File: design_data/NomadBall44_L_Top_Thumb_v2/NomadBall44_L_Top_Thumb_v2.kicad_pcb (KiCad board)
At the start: 2 copper layers, 65.4 x 33.6 mm, 5 parts, among them SW21 SW_Push, SW22 SW_Push, SW23 SW_Push

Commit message: トッププレートのネジ穴フットプリントを変更
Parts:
- REF** (x2): footprint NomadBall44:m2_Screw_Hole_EdgeCuts -> NomadBall44:m2_Screw_Hole
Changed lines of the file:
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@@
 	)
 	(net 0 "")
-	(footprint "NomadBall44:m2_Screw_Hole_EdgeCuts"
+	(footprint "NomadBall44:m2_Screw_Hole"
 		(layer "F.Cu")
 		(at 230.94 119.92)
@@
 			(at 0 -3.2 0)
 			(layer "F.Fab")
-			(hide yes)
 			(effects
 				(font
@@
 			(at 0 3.2 0)
 			(layer "F.Fab")
-			(hide yes)
 			(effects
 				(font
@@
 		(fp_circle
 			(center 0 0)
-			(end 1.1 0)
-			(stroke
-				(width 0.01)
+			(end 2.2 0)
+			(stroke
+				(width 0.15)
 				(type solid)
 			)
 			(fill no)
-			(layer "Edge.Cuts")
+			(layer "Cmts.User")
+		)
+		(fp_circle
+			(center 0 0)
+			(end 2.45 0)
+			(stroke
+				(width 0.05)
+				(type solid)
+			)
+			(fill no)
+			(layer "F.CrtYd")
 		)
 		(fp_text user "${REFERENCE}"
-			(at 0 0 0)
-			(layer "F.Fab")
-			(effects
-				(font
-					(size 1 1)
-					(thickness 0.15)
-				)
-			)
+			(at 0.3 0 0)
+			(layer "F.Fab")
+			(effects
+				(font
+					(size 1 1)
+					(thickness 0.15)
+				)
+			)
+		)
+		(pad "" np_thru_hole circle
+			(at 0 0)
+			(size 2.2 2.2)
+			(drill 2.2)
+			(layers "*.Cu" "*.Mask")
 		)
 		(embedded_fonts no)
@@
 		(embedded_fonts no)
 	)
-	(footprint "NomadBall44:m2_Screw_Hole_EdgeCuts"
+	(footprint "NomadBall44:m2_Screw_Hole"
 		(layer "F.Cu")
 		(at 258.434757 133.419999)
@@
 			(at 0 -3.2 0)
 			(layer "F.Fab")
-			(hide yes)
 			(effects
 				(font
@@
 			(at 0 3.2 0)
 			(layer "F.Fab")
-			(hide yes)
 			(effects
 				(font
@@
 		(fp_circle
 			(center 0 0)
-			(end 1.1 0)
-			(stroke
-				(width 0.01)
+			(end 2.2 0)
+			(stroke
+				(width 0.15)
 				(type solid)
 			)
 			(fill no)
-			(layer "Edge.Cuts")
+			(layer "Cmts.User")
+		)
+		(fp_circle
+			(center 0 0)
+			(end 2.45 0)
+			(stroke
+				(width 0.05)
+				(type solid)
+			)
+			(fill no)
+			(layer "F.CrtYd")
 		)
 		(fp_text user "${REFERENCE}"
-			(at 0 0 0)
-			(layer "F.Fab")
-			(effects
-				(font
-					(size 1 1)
-					(thickness 0.15)
-				)
-			)
+			(at 0.3 0 0)
+			(layer "F.Fab")
+			(effects
+				(font
+					(size 1 1)
+					(thickness 0.15)
+				)
+			)
+		)
+		(pad "" np_thru_hole circle
+			(at 0 0)
+			(size 2.2 2.2)
+			(drill 2.2)
+			(layers "*.Cu" "*.Mask")
 		)
 		(embedded_fonts no)

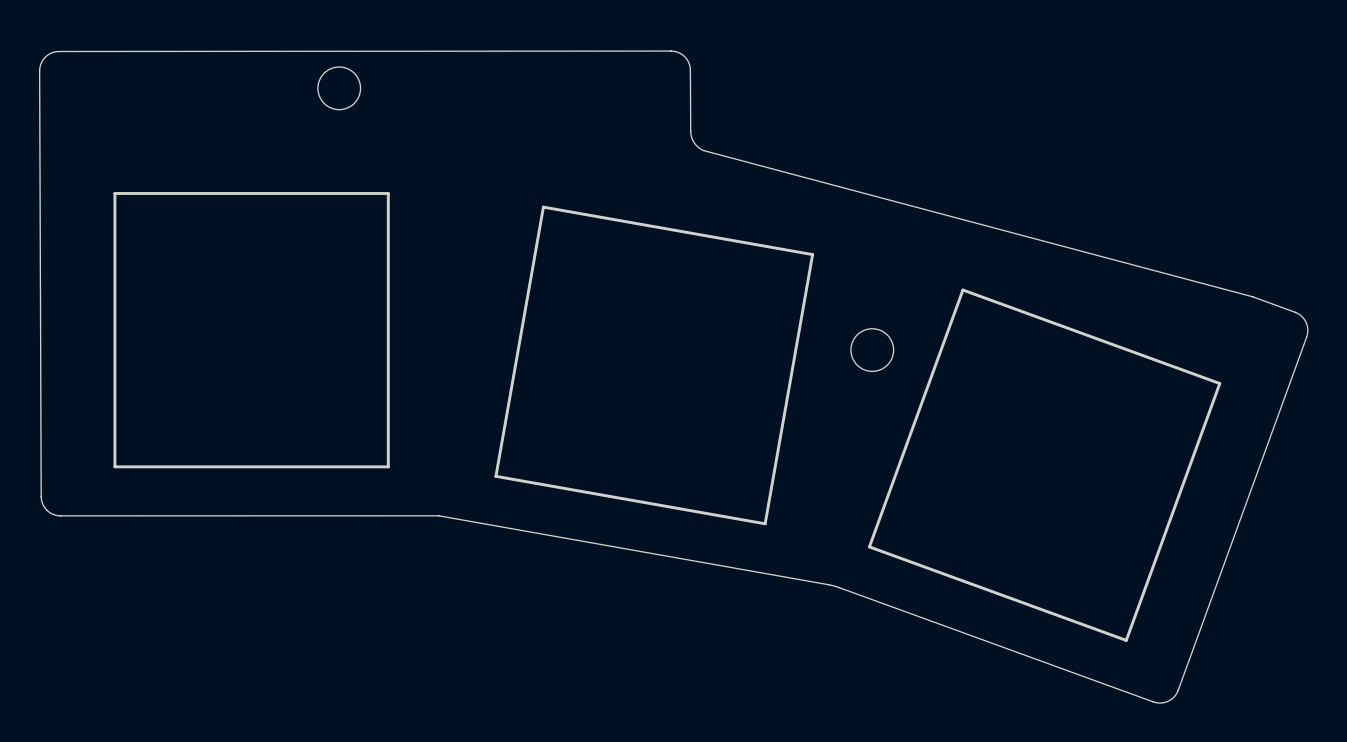
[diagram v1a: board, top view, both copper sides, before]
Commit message: トッププレートの外形線を微修正
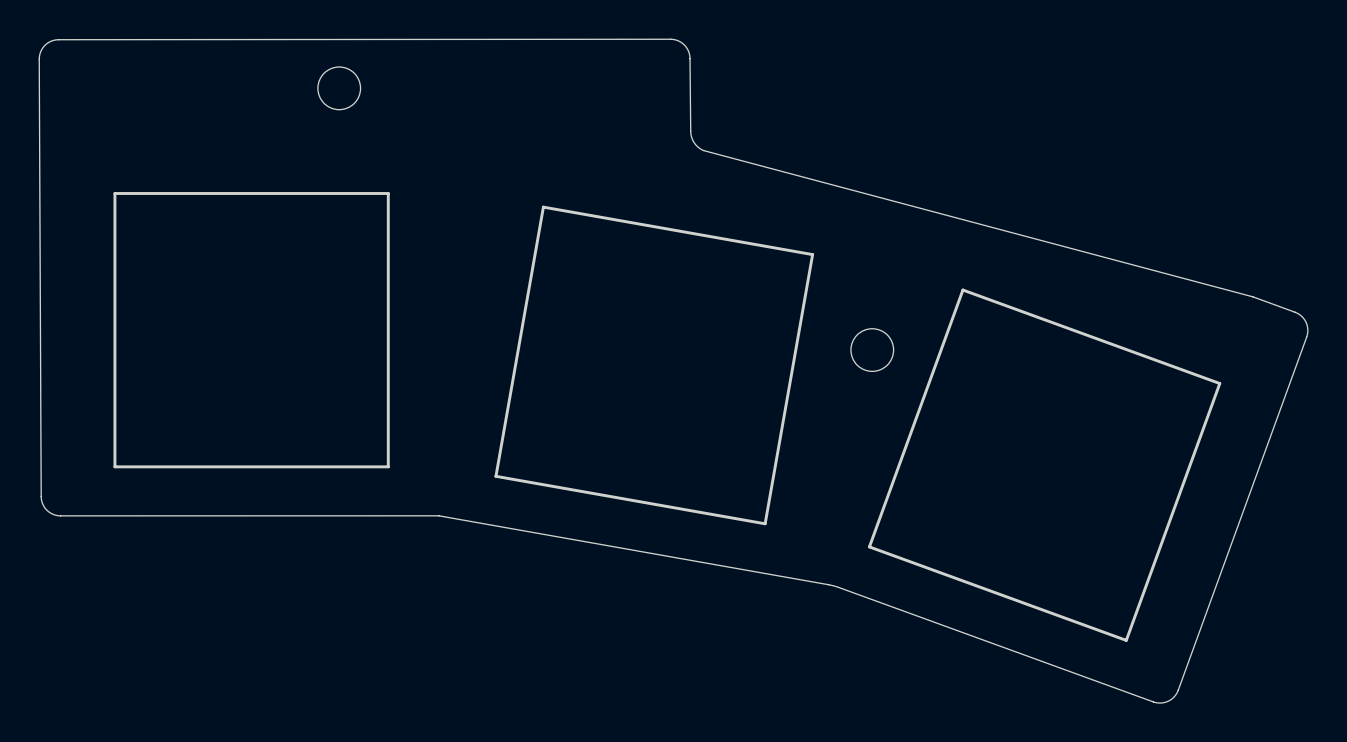
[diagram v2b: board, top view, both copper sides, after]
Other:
- board size 65.4 x 33.6 mm -> 65.4 x 34.2 mm
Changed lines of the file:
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@@
 	)
 	(gr_line
-		(start 215.487107 119.02)
+		(start 215.467107 118.41)
 		(end 215.567107 140.9729)
 		(stroke
@@
 	)
 	(gr_arc
-		(start 248.052893 117.997107)
-		(mid 248.76 118.29)
-		(end 249.052893 118.997107)
+		(start 248.032893 117.388553)
+		(mid 248.740002 117.681444)
+		(end 249.032893 118.388553)
 		(stroke
 			(width 0.05)
@@
 	)
 	(gr_arc
-		(start 215.487107 119.02)
-		(mid 215.78 118.312893)
-		(end 216.487107 118.02)
+		(start 215.467107 118.411446)
+		(mid 215.760001 117.704342)
+		(end 216.467107 117.411446)
 		(stroke
 			(width 0.05)
@@
 	)
 	(gr_line
-		(start 216.487107 118.02)
-		(end 248.052893 117.997107)
+		(start 216.467107 117.411446)
+		(end 248.032893 117.388553)
 		(stroke
 			(width 0.05)
@@
 	)
 	(gr_line
-		(start 249.052893 118.9971)
+		(start 249.032846 118.388553)
 		(end 249.069999 122.13)
 		(stroke
